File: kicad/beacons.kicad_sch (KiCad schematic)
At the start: 50 parts, among them IC1 AP7179DSKZ20-13, IC2 AP7179DSKZ20-13, J1 USB_C_Receptacle_USB2.0_16P, J2 Conn_01x03, J3 Conn_01x18, J4 Conn_01x02, SW1 SW_Push, SW2 SW_Push, SW3 SW_SPST, U1 ESP32-S3-WROOM-1, U2 SN74LVC1T45DCK, U3 74HC595, U4 MAX17048G+T10, U5 MCP73831-2-OT

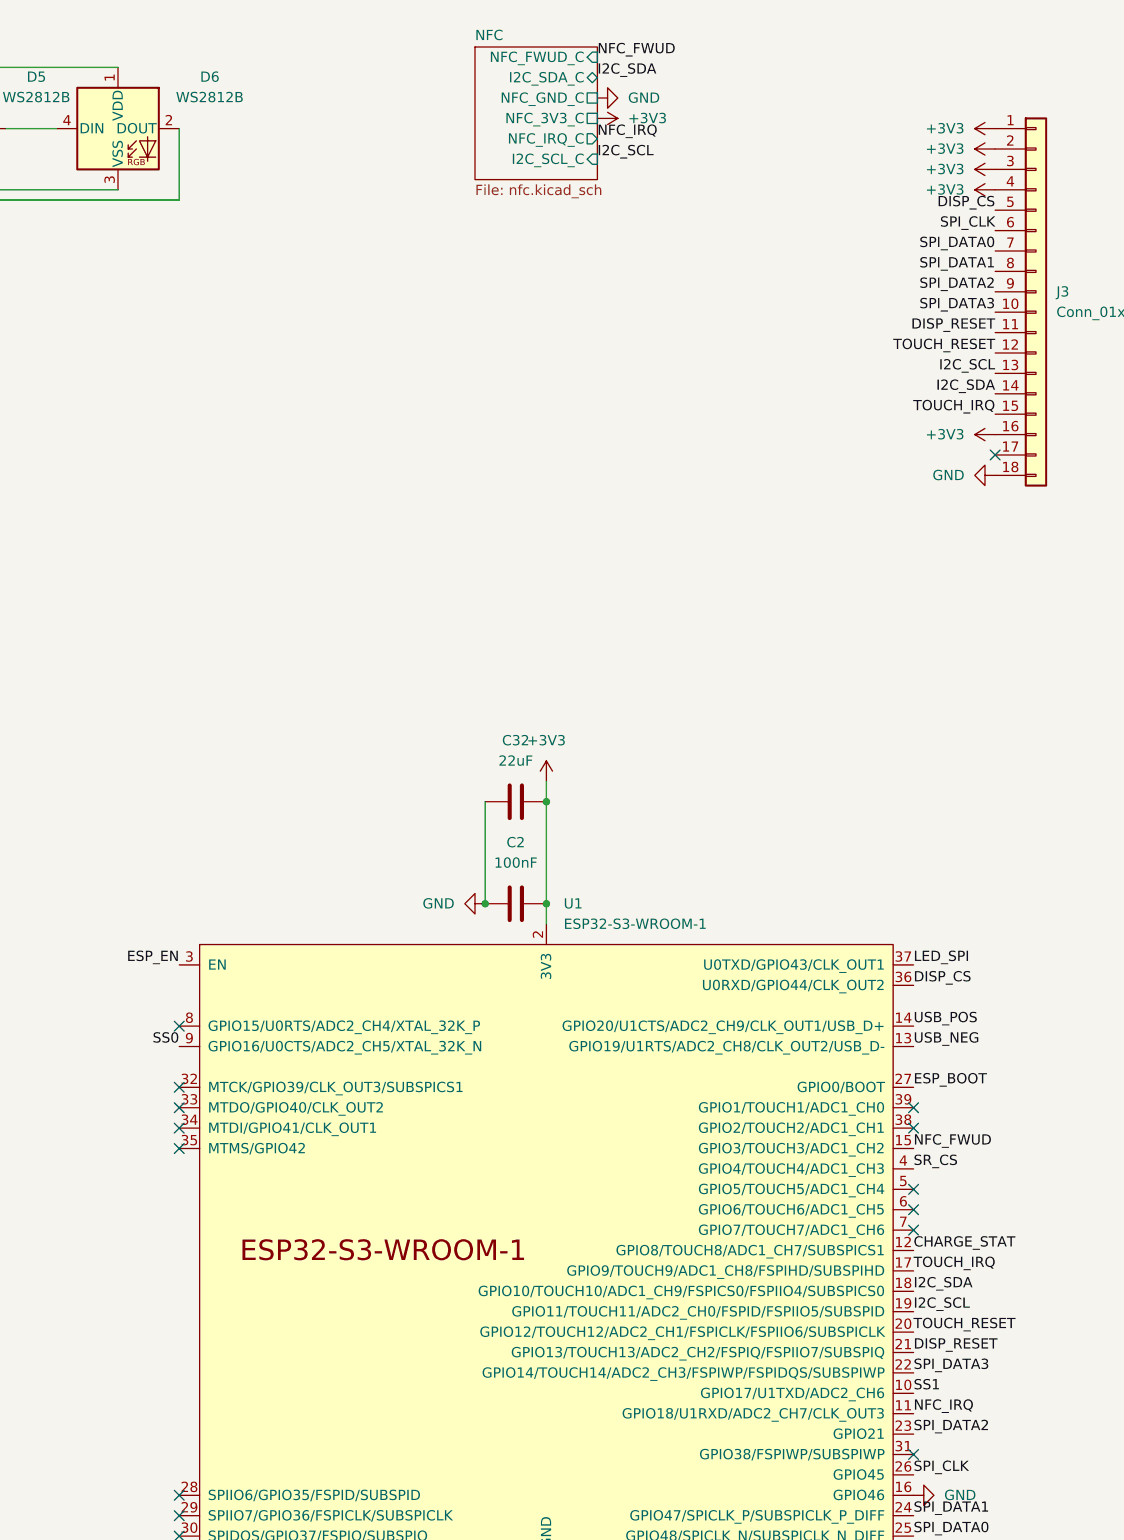
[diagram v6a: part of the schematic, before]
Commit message: Added NFC enable pin
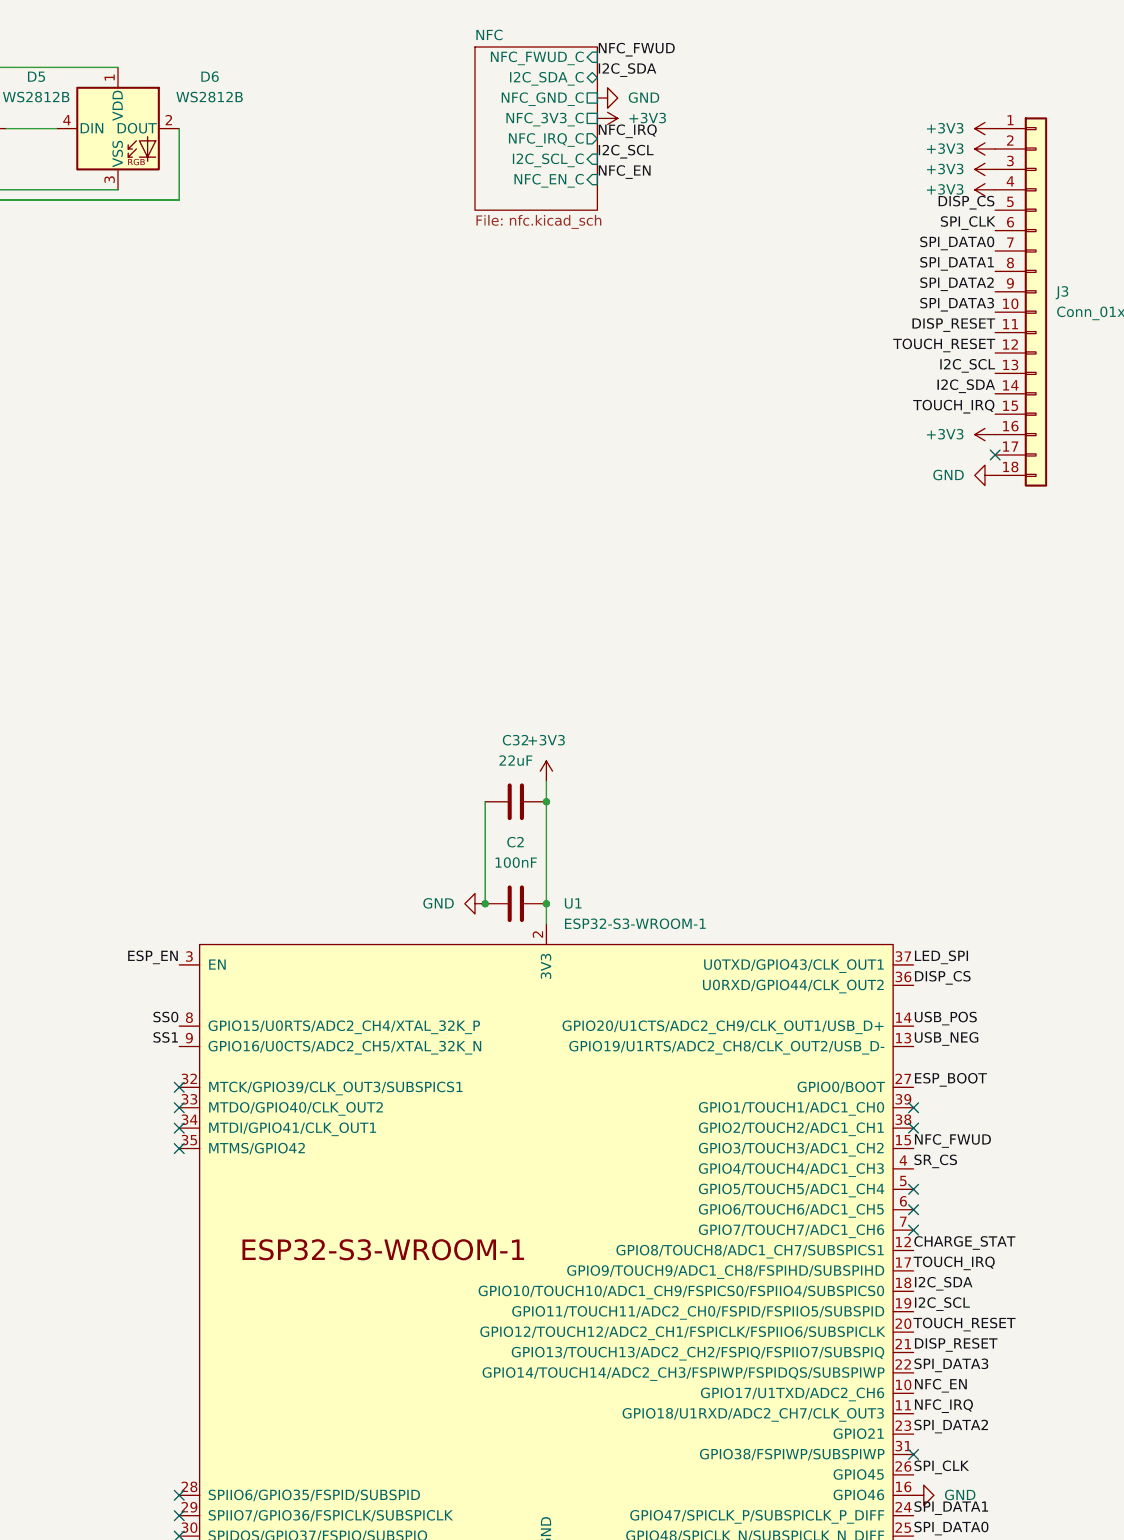
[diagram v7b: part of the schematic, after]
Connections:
- net SS0: now also U1.8 (GPIO15/U0RTS/ADC2_CH4/XTAL_32K_P); no longer U1.9 (GPIO16/U0CTS/ADC2_CH5/XTAL_32K_N)
- net SS1: now also U1.9 (GPIO16/U0CTS/ADC2_CH5/XTAL_32K_N); no longer U1.10 (GPIO17/U1TXD/ADC2_CH6)
- new net NFC_EN: U1.10 (GPIO17/U1TXD/ADC2_CH6)
- no-connect marks 45 -> 44
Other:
- sheet NFC ports: added NFC_EN_C; removed none
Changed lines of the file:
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@@
 	)
 	(no_connect
-		(at 130.81 144.78)
-	)
-	(no_connect
 		(at 222.25 170.18)
 	)
@@
 		)
 	)
-	(label "SS0"
-		(at 130.81 147.32 180)
-		(effects
-			(font
-				(size 1.27 1.27)
-			)
-			(justify right bottom)
-		)
-	)
 	(label "NFC_IRQ"
 		(at 182.88 34.29 0)
@@
 		)
 	)
+	(label "SS1"
+		(at 130.81 147.32 180)
+		(effects
+			(font
+				(size 1.27 1.27)
+			)
+			(justify right bottom)
+		)
+	)
 	(label "I2C_SCL"
 		(at 182.88 36.83 0)
@@
 		)
 	)
+	(label "SS0"
+		(at 130.81 144.78 180)
+		(effects
+			(font
+				(size 1.27 1.27)
+			)
+			(justify right bottom)
+		)
+	)
 	(label "DISP_CS"
 		(at 232.41 43.18 180)
@@
 		)
 	)
+	(label "NFC_EN"
+		(at 182.88 39.37 0)
+		(effects
+			(font
+				(size 1.27 1.27)
+			)
+			(justify left bottom)
+		)
+	)
 	(label "LED_PEAK"
 		(at 27.94 64.77 0)
@@
 		)
 	)
+	(label "NFC_EN"
+		(at 222.25 190.5 0)
+		(effects
+			(font
+				(size 1.27 1.27)
+			)
+			(justify left bottom)
+		)
+	)
 	(label "SPI_DATA1"
 		(at 222.25 205.74 0)
@@
 		)
 	)
-	(label "SS1"
-		(at 222.25 190.5 0)
-		(effects
-			(font
-				(size 1.27 1.27)
-			)
-			(justify left bottom)
-		)
-	)
 	(label "SS0"
 		(at 370.84 60.96 0)
@@
 	(sheet
 		(at 167.64 22.86)
-		(size 15.24 16.51)
+		(size 15.24 20.32)
 		(exclude_from_sim no)
 		(in_bom yes)
@@
 		)
 		(property "Sheetfile" "nfc.kicad_sch"
-			(at 167.64 39.9546 0)
+			(at 167.64 43.7646 0)
 			(effects
 				(font
@@
 			(effects
 				(font
+					(size 1.27 1.27)
+				)
+				(justify right)
+			)
+		)
+		(pin "NFC_EN_C" input
+			(at 182.88 39.37 0)
+			(effects
+				(font
